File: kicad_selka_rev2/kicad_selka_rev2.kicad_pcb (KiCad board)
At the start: 2 copper layers, 88 x 206.9 mm, 104 parts, among them J1 Conn_01x02_Pin, J10 Conn_01x01_Pin, J11 Conn_01x01_Pin, J12 Conn_01x01_Pin, J13 Conn_01x01_Pin, J14 Conn_01x01_Pin, J15 Conn_01x01_Pin, J16 Conn_01x01_Pin, J17 Conn_01x01_Pin, J18 Conn_01x01_Pin, J19 Conn_01x01_Pin, J2 Conn_01x01_Pin, J20 Conn_01x01_Pin, J3 Conn_01x01_Pin, J4 Conn_01x06_Pin, J5 Conn_01x01_Pin, J6 Conn_01x01_Pin, J7 Conn_01x01_Pin, J8 Conn_01x01_Pin, J9 Conn_01x01_Pin, Q1 NPN, U1 ATtiny861A-S

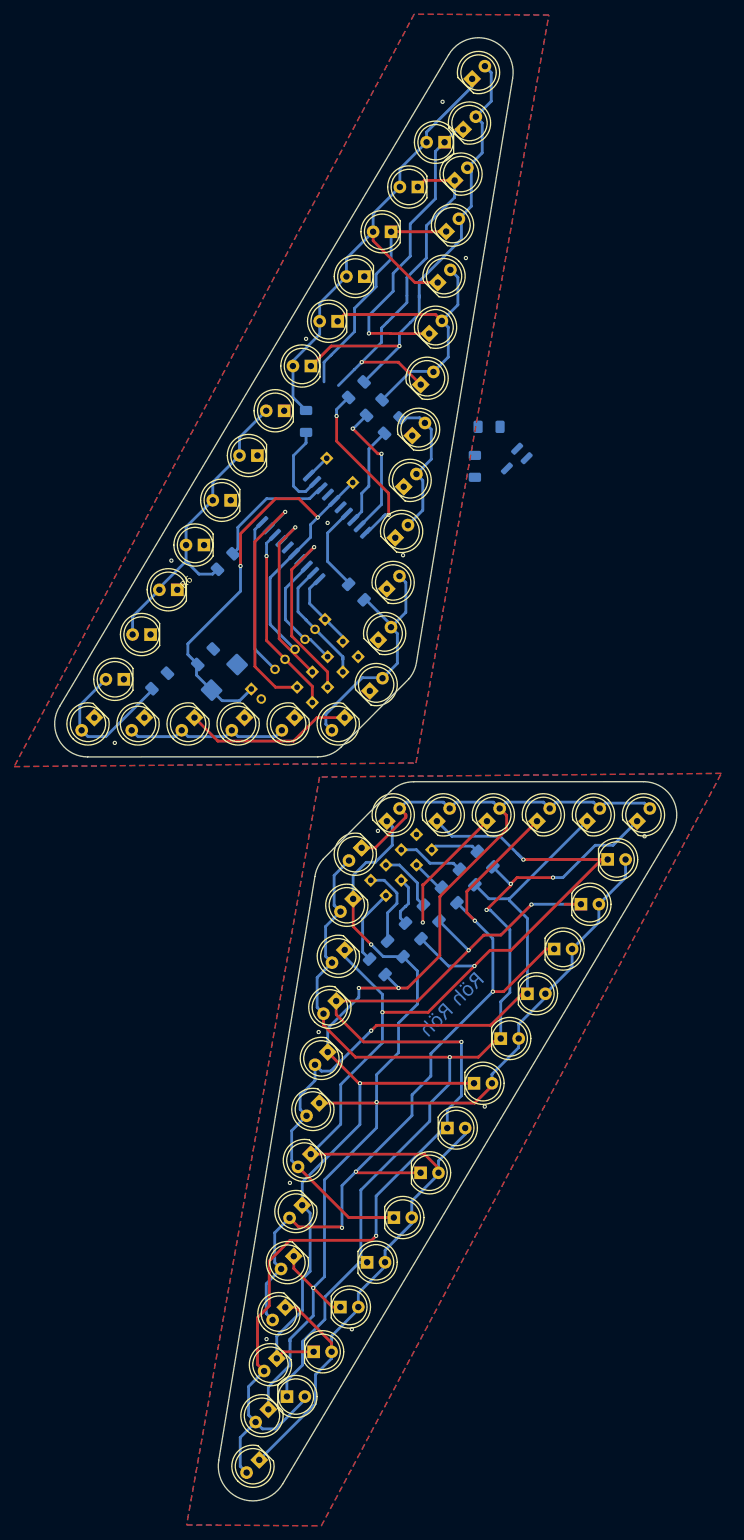
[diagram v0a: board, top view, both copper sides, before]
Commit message: Lisää putsausta ja selkäsalaman muutosta
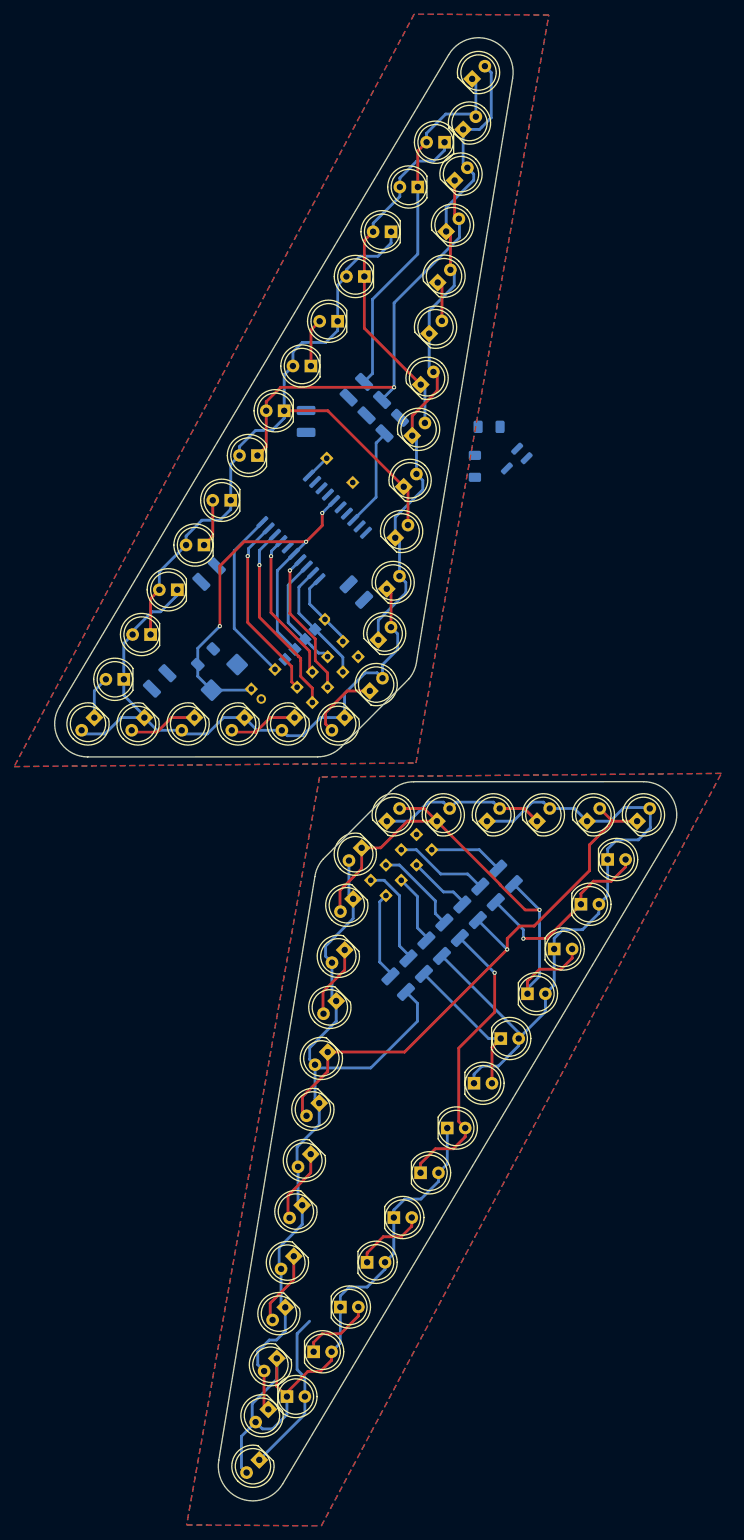
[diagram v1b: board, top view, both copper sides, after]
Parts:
- C1: value 10 u -> 10u
- J4: footprint Connector_PinHeader_2.00mm:PinHeader_1x06_P2.00mm_Horizontal -> Library_zani:PinHeader_1x06_P2.00mm_Horizontal_with_SMD
- R1, R10, R11, R12, R13, R14, R2, R5, R6, R7, R8, R9: footprint Resistor_SMD:R_1206_3216Metric_Pad1.30x1.75mm_HandSolder -> Resistor_SMD:R_1210_3225Metric_Pad1.30x2.65mm_HandSolder
- R3: value R -> 50; footprint Resistor_SMD:R_1206_3216Metric_Pad1.30x1.75mm_HandSolder -> Resistor_SMD:R_1210_3225Metric_Pad1.30x2.65mm_HandSolder
- R4: value R50 -> 50; footprint Resistor_SMD:R_1206_3216Metric_Pad1.30x1.75mm_HandSolder -> Resistor_SMD:R_1210_3225Metric_Pad1.30x2.65mm_HandSolder
- moved R10 3.84 mm to (144.6, 156.8)
- moved R12 3.84 mm to (139.5, 161.9)
- moved R13 3.84 mm to (137.0, 164.4)
- moved R9 3.84 mm to (147.1, 154.3)
- moved R11 3.84 mm to (142.1, 159.3)
- moved R8 3.84 mm to (149.7, 151.7)
- moved R14 3.84 mm to (134.4, 167.0)
- moved R6 2.90 mm to (107.7, 109.0)
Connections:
- net Net-(J4-Pin_1) renamed /MOSI
- net Net-(J4-Pin_2) renamed /MISO
- net Net-(J4-Pin_3) renamed /SCK
- net Net-(J4-Pin_6) renamed /RESET
- D10 pad 1: Net-(D10-K) -> Net-(D1-A)
- D11 pad 1: Net-(D1-K) -> Net-(D11-K)
- D11 pad 2: Net-(D11-A) -> Net-(D1-A)
- D12 pad 1: Net-(D12-K) -> Net-(D1-A)
- D12 pad 2: Net-(D11-A) -> Net-(D11-K)
- D13 pad 1: Net-(D10-K) -> Net-(D1-K)
- D13 pad 2: Net-(D11-A) -> Net-(D11-K)
- D15 pad 1: Net-(D15-K) -> Net-(D14-A)
- D15 pad 2: Net-(D14-A) -> Net-(D14-K)
- D17 pad 1: Net-(D17-K) -> Net-(D14-A)
- D17 pad 2: Net-(D14-A) -> Net-(D16-K)
- D18 pad 1: Net-(D14-K) -> Net-(D18-K)
- D18 pad 2: Net-(D18-A) -> Net-(D14-A)
- D19 pad 1: Net-(D15-K) -> Net-(D14-A)
- D19 pad 2: Net-(D18-A) -> Net-(D18-K)
- D2 pad 1: Net-(D12-K) -> Net-(D1-A)
- D2 pad 2: Net-(D1-A) -> Net-(D1-K)
- D20 pad 1: Net-(D16-K) -> Net-(D20-K)
- D20 pad 2: Net-(D18-A) -> Net-(D14-A)
- D21 pad 1: Net-(D14-K) -> Net-(D14-A)
- D21 pad 2: Net-(D21-A) -> Net-(D20-K)
- D22 pad 1: Net-(D15-K) -> Net-(D22-K)
- D22 pad 2: Net-(D21-A) -> Net-(D14-A)
- D23 pad 1: Net-(D16-K) -> Net-(D14-A)
- D23 pad 2: Net-(D21-A) -> Net-(D22-K)
- D24 pad 1: Net-(D14-K) -> Net-(D24-K)
- D24 pad 2: Net-(D17-K) -> Net-(D14-A)
- D25 pad 1: Net-(D15-K) -> Net-(D14-A)
- D25 pad 2: Net-(D17-K) -> Net-(D24-K)
- D26 pad 1: Net-(D16-K) -> Net-(D14-K)
- D26 pad 2: Net-(D17-K) -> Net-(D24-K)
- D27 pad 1: Net-(D14-A) -> Net-(D24-K)
- D27 pad 2: Net-(D17-K) -> Net-(D14-K)
- D28 pad 1: Net-(D14-K) -> Net-(D16-K)
- D28 pad 2: Net-(D16-K) -> Net-(D24-K)
- D29 pad 1: Net-(D15-K) -> Net-(D24-K)
- D3 pad 1: Net-(D10-K) -> Net-(D3-K)
- D30 pad 1: Net-(D14-A) -> Net-(D18-K)
- D30 pad 2: Net-(D16-K) -> Net-(D24-K)
- D31 pad 1: Net-(D18-A) -> Net-(D24-K)
- D31 pad 2: Net-(D16-K) -> Net-(D18-K)
- D32 pad 1: Net-(D21-A) -> Net-(D20-K)
- D32 pad 2: Net-(D16-K) -> Net-(D24-K)
- D33 pad 1: Net-(D17-K) -> Net-(D24-K)
- D33 pad 2: Net-(D16-K) -> Net-(D20-K)
- D34 pad 1: Net-(D14-K) -> Net-(D22-K)
- D34 pad 2: Net-(D15-K) -> Net-(D24-K)
- D35 pad 1: Net-(D14-A) -> Net-(D24-K)
- D35 pad 2: Net-(D15-K) -> Net-(D22-K)
- D36 pad 1: Net-(D18-A) -> Net-(D14-K)
- D36 pad 2: Net-(D15-K) -> Net-(D22-K)
- D37 pad 1: Net-(D21-A) -> Net-(D22-K)
- D37 pad 2: Net-(D15-K) -> Net-(D14-K)
- D38 pad 1: Net-(D17-K) -> Net-(D16-K)
- D38 pad 2: Net-(D15-K) -> Net-(D22-K)
- D39 pad 1: Net-(D16-K) -> Net-(D22-K)
- D39 pad 2: Net-(D15-K) -> Net-(D16-K)
- D4 pad 1: Net-(D11-A) -> Net-(D1-A)
- D4 pad 2: Net-(D1-A) -> Net-(D3-K)
- D40 pad 1: Net-(D14-A) -> Net-(D18-K)
- D40 pad 2: Net-(D14-K) -> Net-(D22-K)
- D41 pad 1: Net-(D18-A) -> Net-(D22-K)
- D41 pad 2: Net-(D14-K) -> Net-(D18-K)
- D42 pad 1: Net-(D21-A) -> Net-(D20-K)
- D42 pad 2: Net-(D14-K) -> Net-(D22-K)
- D43 pad 1: Net-(D17-K) -> Net-(D22-K)
- D43 pad 2: Net-(D14-K) -> Net-(D20-K)
- D44 pad 1: Net-(D16-K) -> Net-(D14-K)
- D44 pad 2: Net-(D14-K) -> Net-(D20-K)
- D45 pad 1: Net-(D15-K) -> Net-(D20-K)
- D46 pad 1: Net-(D1-A) -> Net-(D11-K)
- D46 pad 2: Net-(D11-A) -> Net-(D1-K)
- D47 pad 1: Net-(D1-K) -> Net-(D3-K)
- D47 pad 2: Net-(D10-K) -> Net-(D11-K)
- D48 pad 1: Net-(D12-K) -> Net-(D11-K)
- D48 pad 2: Net-(D10-K) -> Net-(D3-K)
- D49 pad 1: Net-(D1-A) -> Net-(D49-K)
- D49 pad 2: Net-(D10-K) -> Net-(D11-K)
- D5 pad 1: Net-(D1-K) -> Net-(D49-K)
- D5 pad 2: Net-(D5-A) -> Net-(D1-A)
- D50 pad 1: Net-(D5-A) -> Net-(D11-K)
- D50 pad 2: Net-(D10-K) -> Net-(D49-K)
- D51 pad 1: Net-(D10-A) -> Net-(D51-K)
- D51 pad 2: Net-(D10-K) -> Net-(D11-K)
- D52 pad 1: Net-(D11-A) -> Net-(D11-K)
- D52 pad 2: Net-(D10-K) -> Net-(D51-K)
- D53 pad 1: Net-(D1-K) -> Net-(D10-A)
- D53 pad 2: Net-(D12-K) -> Net-(D11-K)
- D54 pad 1: Net-(D1-A) -> Net-(D11-K)
- D54 pad 2: Net-(D12-K) -> Net-(D10-A)
- D55 pad 1: Net-(D5-A) -> Net-(D1-K)
- D55 pad 2: Net-(D12-K) -> Net-(D10-A)
- D56 pad 2: Net-(D12-K) -> Net-(D1-K)
- D57 pad 1: Net-(D11-A) -> Net-(D3-K)
- D57 pad 2: Net-(D12-K) -> Net-(D10-A)
- D58 pad 1: Net-(D10-K) -> Net-(D10-A)
- D58 pad 2: Net-(D12-K) -> Net-(D3-K)
- D59 pad 1: Net-(D1-A) -> Net-(D49-K)
- D59 pad 2: Net-(D1-K) -> Net-(D10-A)
- D6 pad 1: Net-(D12-K) -> Net-(D1-A)
- D6 pad 2: Net-(D5-A) -> Net-(D49-K)
- D60 pad 1: Net-(D5-A) -> Net-(D10-A)
- D60 pad 2: Net-(D1-K) -> Net-(D49-K)
- D61 pad 1: Net-(D10-A) -> Net-(D51-K)
- D61 pad 2: Net-(D1-K) -> Net-(D10-A)
- D62 pad 1: Net-(D11-A) -> Net-(D10-A)
- D62 pad 2: Net-(D1-K) -> Net-(D51-K)
- D63 pad 1: Net-(D10-K) -> Net-(D1-K)
- D63 pad 2: Net-(D1-K) -> Net-(D51-K)
- D64 pad 1: Net-(D12-K) -> Net-(D51-K)
- D7 pad 1: Net-(D10-K) -> Net-(D51-K)
- D7 pad 2: Net-(D5-A) -> Net-(D1-A)
- D8 pad 1: Net-(D1-K) -> Net-(D1-A)
- D8 pad 2: Net-(D10-A) -> Net-(D51-K)
- D9 pad 1: Net-(D12-K) -> Net-(D10-A)
- D9 pad 2: Net-(D10-A) -> Net-(D1-A)
- J19 pad 1: +5V -> /GND
- J20 pad 1: Net-(J20-Pin_1) -> /N&VPK
- J4 pad 4: +5V -> /5V
- Q1 pad 3: GND1 -> /GND
- R1 pad 2: Net-(D1-A) -> Net-(D1-K)
- R10 pad 2: Net-(D21-A) -> Net-(D18-K)
- R11 pad 2: Net-(D17-K) -> Net-(D20-K)
- R12 pad 2: Net-(D16-K) -> Net-(D22-K)
- R13 pad 2: Net-(D15-K) -> Net-(D24-K)
- R14 pad 2: Net-(D14-K) -> Net-(D14-A)
- R15 pad 1: Net-(J20-Pin_1) -> Net-(Q1-B)
- R15 pad 2: Net-(Q1-B) -> /N&VPK
- R17 pad 2: +5V -> /5V
- R2 pad 2: Net-(D5-A) -> Net-(D3-K)
- R3 pad 2: Net-(D10-A) -> Net-(D49-K)
- R4 pad 2: Net-(D11-A) -> Net-(D51-K)
- R5 pad 2: Net-(D10-K) -> Net-(D10-A)
- R6 pad 2: Net-(D12-K) -> Net-(D11-K)
- R7 pad 2: Net-(D1-K) -> Net-(D1-A)
- R8 pad 2: Net-(D14-A) -> Net-(D14-K)
- R9 pad 2: Net-(D18-A) -> Net-(D16-K)
- U1 pad 11: Net-(J20-Pin_1) -> /N&VPK
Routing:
- net Net-(D17-K): track 180.2 -> 0.00 mm, vias 5 -> 0
- net Net-(D15-K): track 177.4 -> 0.00 mm, vias 3 -> 0
- net Net-(D16-K): track 201.7 -> 48.2 mm, vias 3 -> 1
- net Net-(D21-A): track 120.9 -> 0.00 mm, vias 4 -> 0
- net Net-(D22-K): track 0.00 -> 106.8 mm
- net Net-(D24-K): track 0.00 -> 105.9 mm
- net Net-(D18-A): track 104.1 -> 0.00 mm, vias 1 -> 0
- net Net-(D10-K): track 96.0 -> 0.00 mm, vias 1 -> 0
- net Net-(D18-K): track 0.00 -> 90.0 mm, vias 0 -> 1
- net Net-(D11-K): track 0.00 -> 90.0 mm
- net Net-(D12-K): track 88.4 -> 0.00 mm, vias 1 -> 0
- net Net-(D10-A): track 20.7 -> 104.4 mm
- net Net-(D20-K): track 0.00 -> 76.7 mm, vias 0 -> 1
- net Net-(D14-K): track 174.0 -> 100.3 mm, vias 3 -> 1
- net Net-(D3-K): track 0.00 -> 72.7 mm, vias 0 -> 1
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
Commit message: hiomista vaille rev
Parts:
- removed J10, J11, J12, J13, J14, J15, J16, J17, J18, J19, J20, J5, J6, J7, J8, J9: Conn_01x01_Pin, Connector_PinHeader_2.00mm:PinHeader_1x01_P2.00mm_Vertical
- removed Q1: NPN, Package_TO_SOT_SMD:SOT-23_Handsoldering
- removed R16, R17: X, Resistor_SMD:R_1206_3216Metric_Pad1.30x1.75mm_HandSolder
- added C2: 100n, Capacitor_SMD:C_0805_2012Metric_Pad1.18x1.45mm_HandSolder, B.Cu at (116.2, 105.5)
- added C3: 100n, Capacitor_SMD:C_0805_2012Metric_Pad1.18x1.45mm_HandSolder, B.Cu at (126.4, 95.2)
- added SW1: PUSH, Connector_PinHeader_2.00mm:PinHeader_1x02_P2.00mm_Vertical, B.Cu at (120.5, 89.4)
- J1: value Conn_01x02_Pin -> Conn_01x02; footprint Connector_PinHeader_2.00mm:PinHeader_1x02_P2.00mm_Vertical -> Connector_PinHeader_2.54mm:PinHeader_1x02_P2.54mm_Vertical
- J2: value Conn_01x01_Pin -> Conn_01x06; footprint Connector_PinHeader_2.00mm:PinHeader_1x01_P2.00mm_Vertical -> footprintteja:PinHeader_1x06_P2.00mm_Horizontal_smd_tht
- J3: value Conn_01x01_Pin -> Conn_01x08; footprint Connector_PinHeader_2.00mm:PinHeader_1x01_P2.00mm_Vertical -> footprintteja:PinHeader_1x08_P2.00mm_Vertical_levee
- J4: value Conn_01x06_Pin -> Conn_01x08; footprint Library_zani:PinHeader_1x06_P2.00mm_Horizontal_with_SMD -> footprintteja:PinHeader_1x08_P2.00mm_Vertical_levee
- R15: value 470 -> X; footprint Resistor_SMD:R_1206_3216Metric_Pad1.30x1.75mm_HandSolder -> Resistor_SMD:R_1210_3225Metric_Pad1.30x2.65mm_HandSolder
- U1: value ATtiny861A-S -> ATtiny861A SOIC20
- moved R15 49.4 mm to (104.6, 121.9), turned to -45 degrees
- moved R5 44.7 mm to (122.1, 84.8), turned to 90 degrees
- moved R4 32.1 mm to (126.5, 79.4), turned to 90 degrees
- moved J3 30.9 mm to (126.6, 116.7), turned to 135 degrees
- moved J4 27.2 mm to (143.9, 133.9)
- moved R6 23.0 mm to (130.5, 106.0), turned to -45 degrees
- moved R7 22.9 mm to (126.9, 109.7), turned to -45 degrees
- moved R14 15.2 mm to (134.4, 151.8), turned to -90 degrees
- moved R8 14.7 mm to (152.5, 137.3)
- moved R9 14.5 mm to (149.8, 140.0)
- moved R10 14.2 mm to (147.0, 142.8)
- moved R11 14.1 mm to (144.2, 145.4)
- moved J1 13.3 mm to (100.4, 126.4), turned to -90 degrees
- moved D17 12.9 mm to (126.9, 156.5)
- moved D18 12.9 mm to (125.7, 163.7)
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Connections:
- net /CPA1 renamed /CA0
- net /CPA2 renamed /CA1
- net /CPA3 renamed /CA2
- net /CPA4 renamed /CA3
- net /CPA5 renamed /CA4
- net /CPA6 renamed /CA5
- net /CPA7 renamed /CA6
- D63 pad 1: Net-(D1-K) -> Net-(D51-K)
- D63 pad 2: Net-(D51-K) -> Net-(D1-K)
- D64 pad 1: Net-(D51-K) -> Net-(D1-K)
- D64 pad 2: Net-(D1-K) -> Net-(D51-K)
- J2 pad 1: GND1 -> /PB0
- J3 pad 1: GND2 -> /PB0
- J4 pad 1: /MOSI -> /CB0
- J4 pad 2: /MISO -> /CB1
- J4 pad 3: /SCK -> /CB2
- J4 pad 4: /5V -> /CB3
- J4 pad 5: GND1 -> /CB4
- J4 pad 6: /RESET -> /CB5
- R10 pad 1: Net-(J10-Pin_1) -> /CB2
- R11 pad 1: Net-(J12-Pin_1) -> /CB3
- R12 pad 1: Net-(J14-Pin_1) -> /CB4
- R13 pad 1: Net-(J16-Pin_1) -> /CB5
- R14 pad 1: Net-(J18-Pin_1) -> /CB6
- R15 pad 1: Net-(Q1-B) -> +5V
- R15 pad 2: /N&VPK -> GND1
- R8 pad 1: Net-(J6-Pin_1) -> /CB0
- R9 pad 1: Net-(J8-Pin_1) -> /CB1
- U1 pad 1: /MOSI -> /PB0
- U1 pad 10: /RESET -> /PB7
- U1 pad 11: /N&VPK -> Net-(U1-PA7)
- U1 pad 2: /MISO -> /PB1
- U1 pad 3: /SCK -> /PB2
- U1 pad 4: Net-(J11-Pin_1) -> /PB3
- U1 pad 7: Net-(J13-Pin_1) -> /PB4
- U1 pad 8: Net-(J15-Pin_1) -> /PB5
- U1 pad 9: Net-(J17-Pin_1) -> /PB6
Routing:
- net GND2: track 0.00 -> 117.5 mm, vias 0 -> 16
- net Net-(D49-K): track 22.3 -> 119.9 mm, vias 0 -> 5
- net Net-(D16-K): track 48.2 -> 137.8 mm, vias 1 -> 2
- net GND1: track 0.00 -> 87.8 mm, vias 0 -> 23
- net Net-(D1-K): track 69.9 -> 153.1 mm, vias 0 -> 3
- net Net-(D51-K): track 55.4 -> 134.4 mm, vias 0 -> 4
- net Net-(D14-K): track 100.3 -> 175.1 mm, vias 1 -> 3
- net Net-(D20-K): track 76.7 -> 131.0 mm, vias 1 -> 3
- net Net-(D3-K): track 72.7 -> 120.3 mm
- net Net-(D22-K): track 106.8 -> 149.7 mm, vias 0 -> 2
- net Net-(D18-K): track 90.0 -> 122.6 mm, vias 1 -> 3
- net /PB6: track 0.00 -> 29.8 mm, vias 0 -> 1
- net /CA3: track 0.00 -> 28.8 mm, vias 0 -> 2
- net /PB4: track 0.00 -> 28.7 mm, vias 0 -> 3
- net Net-(J15-Pin_1): track 27.7 -> 0.00 mm, vias 1 -> 0
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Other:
- board size 88 x 206.9 mm -> 89.2 x 194.1 mm
- board text added: "MASTER"
- board text added: "SLAVE"
